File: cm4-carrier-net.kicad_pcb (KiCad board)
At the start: 4 copper layers, 91.4 x 50.4 mm, 68 parts, among them J1 USB_C_Receptacle_USB2.0, J2 Micro_SD_Card, J3 Abracon_ARJM11-502, J5 block, J6 USB_A, J8 Conn_01x15_MountingPin, Q1 DMP2066LSN, Q2 FDMT800152DC, Q3 FDMT800152DC, SW1 BOOT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

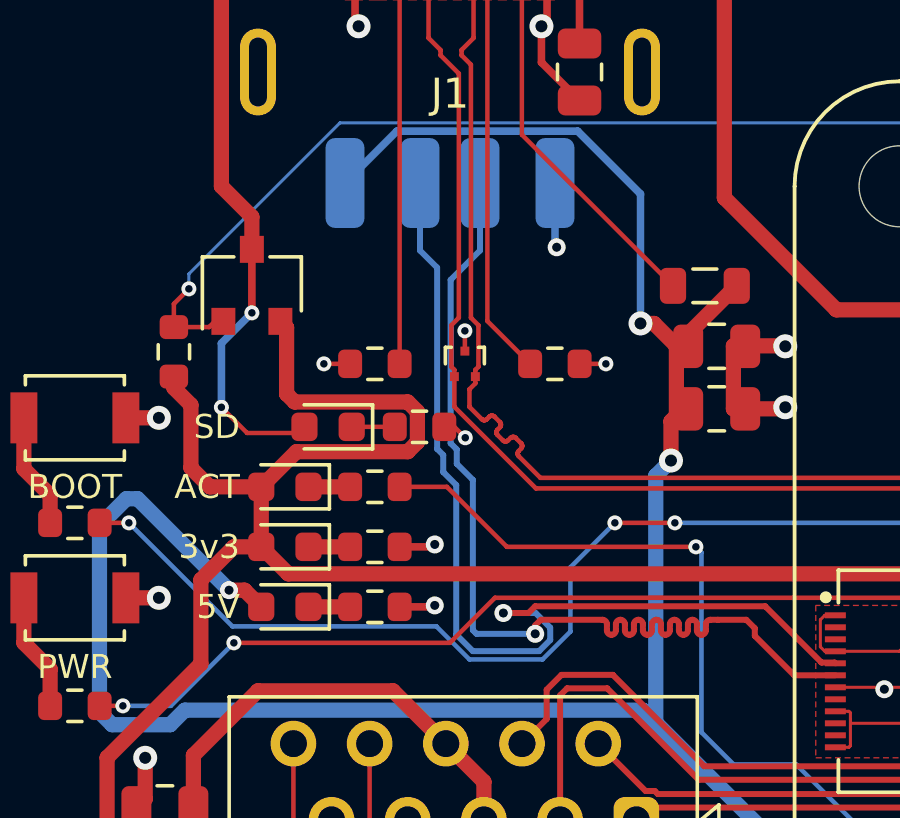
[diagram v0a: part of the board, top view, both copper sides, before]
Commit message: added tvs on the usb a
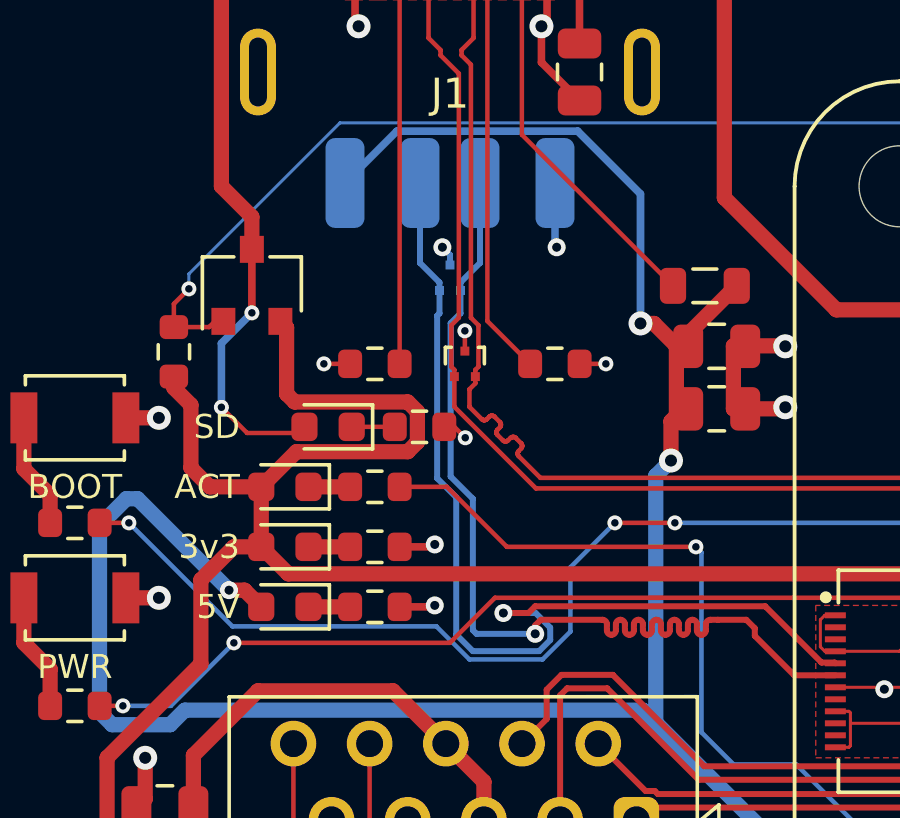
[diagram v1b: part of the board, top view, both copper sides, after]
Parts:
- added U4: TPD2EUSB30, Package_TO_SOT_SMD:Texas_DRT-3, B.Cu at (95.5, 100.3)
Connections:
- net /I2C1_SCL- renamed /I2C1_SCL0-
- net /I2C1_SDA+ renamed /I2C1_SDA0+
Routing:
- net GND: track 173.0 -> 173.7 mm, vias 55 -> 56

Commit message: added some fun thingies
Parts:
- added C12: 22u, Capacitor_SMD:C_0805_2012Metric, F.Cu at (145.8, 87.6)
- added C13: 22u, Capacitor_SMD:C_0805_2012Metric, B.Cu at (85.4, 118.4)
- added M1: Fan, Connector_PinHeader_2.54mm:PinHeader_1x02_P2.54mm_Vertical, F.Cu at (82.3, 118.4)
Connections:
- J8 pad MP: unconnected-(J8-MountPin-PadMP) -> GND
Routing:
- net +5V: track 134.1 -> 140.2 mm
- net +3.3V: track 207.3 -> 213.0 mm
- net GND: track 173.7 -> 178.3 mm, vias 56 -> 61
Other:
- board text added: "5v"
- board text added: "FAN"

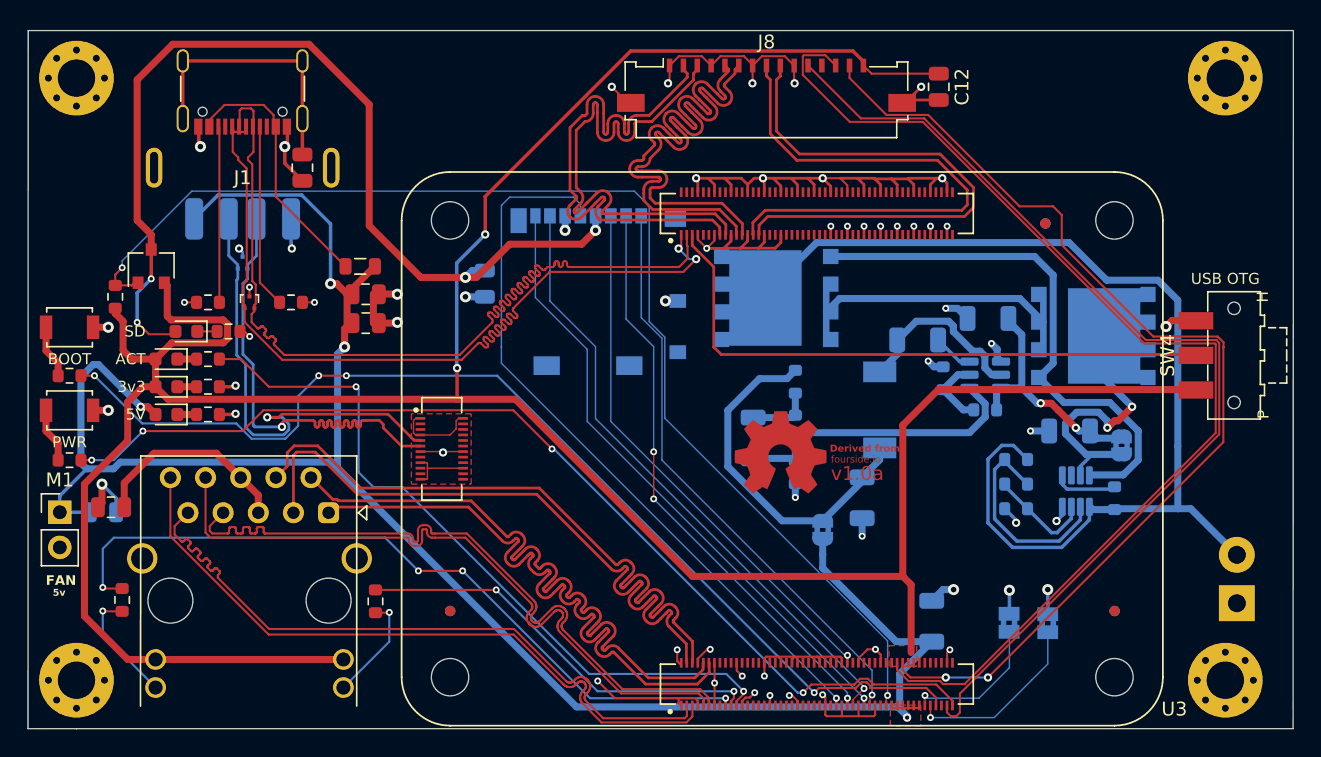
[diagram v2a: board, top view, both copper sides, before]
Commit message: redesigned pcb
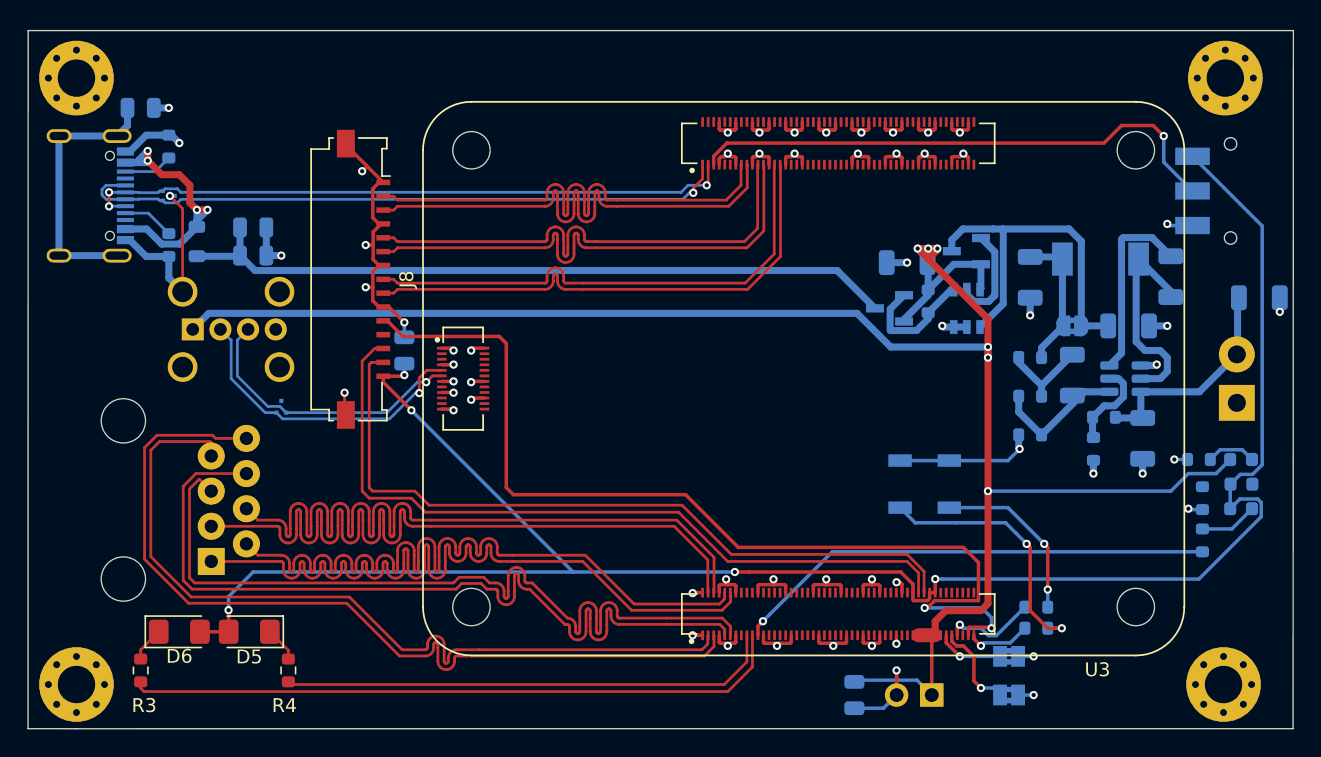
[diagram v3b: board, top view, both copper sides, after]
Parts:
- removed C3: 100n, Capacitor_SMD:C_0805_2012Metric
- removed D4: SD ON, LED_SMD:LED_0603_1608Metric
- removed FID1, FID2, FID3, FID4, FID5, FID6: Fiducial, Fiducial:Fiducial_0.75mm_Mask1.5mm
- removed J2: Micro_SD_Card, Connector_Card:microSD_HC_Molex_104031-0811
- removed JP5: SolderJumper_2_Bridged, Jumper:SolderJumper-2_P1.3mm_Bridged2Bar_RoundedPad1.0x1.5mm
- removed LOGO1: Logo_Open_Hardware_Small, Symbol:OSHW-Symbol_6.7x6mm_Copper
- removed Q1: DMP2066LSN, Package_TO_SOT_SMD:SC-59
- removed R12, R8: 220R, Resistor_SMD:R_0603_1608Metric
- removed R18: 2740kOhm, Resistor_SMD:R_0603_1608Metric
- removed R19: 215kOhm, Resistor_SMD:R_0603_1608Metric
- removed R20: 84.5kOhm, Resistor_SMD:R_0603_1608Metric
- removed U2: LTC4365TS8, Package_TO_SOT_SMD:TSOT-23-8
- added D5: LED, Diode_SMD:D_1206_3216Metric_Pad1.42x1.75mm_HandSolder, F.Cu at (96.0, 127.0)
- added D6: LED, Diode_SMD:D_1206_3216Metric_Pad1.42x1.75mm_HandSolder, F.Cu at (90.9, 127.0)
- added Q4: IRLML6401TRPBF, digikey-footprints:SOT-23-3, B.Cu at (142.2, 103.6)
- C1, C12, C2, C5, D1, D2, D3, FB1, M1, R1, R10, R11, R2, R6, R7, R9, SW1, SW2, SW4, U6: moved to B.Cu
- C4: value 22u -> 22uF; footprint Capacitor_SMD:C_0805_2012Metric -> Capacitor_SMD:C_1206_3216Metric
- J1: footprint jkiv-library:USB_C_Receptacle_GCT-USB4105 -> Connector_USB:USB_C_Receptacle_G-Switch_GT-USB-7010ASV; moved to B.Cu
- J3: value Abracon_ARJM11-502 -> 54602-908LF; footprint jkiv-library:RJ45_Abracon_ARJM11 -> digikey-footprints:Ethernet_Jack_54602-908LF; moved to B.Cu
- J6: footprint Connector_USB:USB_A_Receptacle_GCT_USB1046 -> Connector_USB:USB_A_Wuerth_614004134726_Horizontal
- Q2: value FDMT800152DC -> LTC4412ES6_TRMPBF; footprint Package_TO_SOT_SMD:PQFN_8x8 -> digikey-footprints:SOT-23-6
- Q3: value FDMT800152DC -> IRLML6401TRPBF; footprint Package_TO_SOT_SMD:PQFN_8x8 -> digikey-footprints:SOT-23-3
- R17: value 510kOhm -> 470kOhm
- moved D3 78.4 mm to (167.6, 118.1)
- moved D2 78.0 mm to (167.7, 116.3)
- moved D1 77.7 mm to (167.6, 114.6)
- moved R10 73.0 mm to (164.8, 120.4), turned to 90 degrees
- moved R7 72.3 mm to (164.8, 117.3), turned to -90 degrees
- moved R9 71.8 mm to (152.8, 125.2), turned to 180 degrees
- moved R6 71.7 mm to (164.6, 114.6), turned to 180 degrees
- moved R11 70.9 mm to (152.8, 126.7), turned to 180 degrees
- moved SW1 64.6 mm to (146.6, 116.3), turned to 90 degrees
- moved M1 64.4 mm to (145.3, 131.6), turned to 90 degrees
- moved SW2 60.2 mm to (143.0, 116.3), turned to 90 degrees
- moved C13 55.9 mm to (139.7, 131.6), turned to -90 degrees
- moved C12 43.1 mm to (107.2, 106.7), turned to 90 degrees
- moved J8 32.1 mm to (104.8, 101.5), turned to -90 degrees
- moved C4 30.5 mm to (143.5, 100.3), turned to 180 degrees
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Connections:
- C1 pad 1: +5V -> 5v_From_USB
- C10 pad 2: +5V -> 5v_From_Bot
- C2 pad 1: +5V -> 5v_From_USB
- C4 pad 1: /SD_PWR -> +5V
- FB1 pad 1: +5V -> 5v_From_USB
- J3 pad 5: Net-(C3-Pad1) -> /E0_TR2+
- J3 pad 6: Net-(C3-Pad1) -> /E0_TR2-
- J3 pad 7: /E0_TR2+ -> /E0_TR3+
- J3 pad 8: /E0_TR2- -> /E0_TR3-
- J5 pad 2: Net-(J5-Pin_2) -> +12V
- JP6 pad 1: +5V -> 5v_From_Bot
- Q2 pad 1: Net-(Q2-G) -> 5v_From_Bot
- Q2 pad 2: Net-(Q2-S) -> GND
- Q2 pad 3: Net-(J5-Pin_2) -> GND
- Q3 pad 1: Net-(Q2-G) -> Net-(Q2-GATE)
- Q3 pad 2: Net-(Q2-S) -> +5V
- Q3 pad 3: Net-(JP5-A) -> 5v_From_Bot
- R17 pad 1: Net-(J5-Pin_2) -> +5V
- R17 pad 2: Net-(U2-~{SHDN}) -> Net-(Q2-STAT)
- R3 pad 1: Net-(J3-Pad14) -> Net-(D6-K)
- R4 pad 1: Net-(J3-Pad12) -> Net-(D5-K)
- U3 pad JP2_100: unconnected-(U3B-HDMI_TXDDC_SCL_PORT-PadJP2_100) -> /HDMI_SCL
- U3 pad JP2_51: unconnected-(U3B-HDMI_CEC_PORT-PadJP2_51) -> /HDMI_CEC
- U3 pad JP2_70: unconnected-(U3B-HDMI_TX2P_PORT-PadJP2_70) -> /HDMI_D2+
- U3 pad JP2_72: unconnected-(U3B-HDMI_TX2N_PORT-PadJP2_72) -> /HDMI_D2-
- U3 pad JP2_76: unconnected-(U3B-HDMI_TX1P_PORT-PadJP2_76) -> /HDMI_D1+
- U3 pad JP2_78: unconnected-(U3B-HDMI_TX1N_PORT-PadJP2_78) -> /HDMI_D1-
- U3 pad JP2_82: unconnected-(U3B-HDMI_TX0P_PORT-PadJP2_82) -> /HDMI_D0+
- U3 pad JP2_84: unconnected-(U3B-HDMI_TX0N_PORT-PadJP2_84) -> /HDMI_D0-
- U3 pad JP2_88: unconnected-(U3B-HDMI_TXCLKP_PORT-PadJP2_88) -> /HDMI_CK+
- U3 pad JP2_90: unconnected-(U3B-HDMI_TXCLKN_PORT-PadJP2_90) -> /HDMI_CK-
- U3 pad JP2_99: unconnected-(U3B-HDMI_TXDDC_SDA_PORT-PadJP2_99) -> /HDMI_SDA
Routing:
- net /SD_PWR_ON: track 87.7 -> 0.00 mm, vias 2 -> 0
- net Net-(J5-Pin_2): track 78.6 -> 0.00 mm
- net +3.3V: track 213.0 -> 139.7 mm, vias 2 -> 5
- net /SD_PWR: track 71.9 -> 0.00 mm, vias 4 -> 0
- net /PI_nRPI_BOOT: track 77.9 -> 6.71 mm, vias 4 -> 1
- net /PI_GLOBAL_EN: track 74.5 -> 4.68 mm, vias 4 -> 1
- net /SD_CLK: track 53.4 -> 0.00 mm, vias 1 -> 0
- net 5v_From_USB: track 0.00 -> 52.6 mm
- net /SD_D1: track 45.4 -> 0.00 mm, vias 1 -> 0
- net /SD_D0: track 45.3 -> 0.00 mm, vias 1 -> 0
- net /SD_D2: track 42.5 -> 0.00 mm, vias 1 -> 0
- net /SD_D3: track 42.2 -> 0.00 mm, vias 3 -> 0
- net /SD_CMD: track 39.7 -> 0.00 mm, vias 1 -> 0
- net Net-(Q2-G): track 39.3 -> 0.00 mm
- net GND: track 178.3 -> 146.7 mm, vias 61 -> 59
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- removed copper zone on F.Cu, net +3.3V
- removed copper zone on F.Cu, net +5V
- removed copper zone on F.Cu, net GND
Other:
- board text removed: "3v3"
- board text removed: "5V"
- board text removed: "5v"
- board text removed: "ACT"
- board text removed: "BOOT"
- board text removed: "Derived from"
- board text removed: "FAN"
- board text removed: "H"
- board text removed: "P"
- board text removed: "PWR"
- board text removed: "SD"
- board text removed: "These should probably be toggles, but I don't feel like making more space for unnecessary things."
- board text removed: "USB OTG"
- board text removed: "fourside.io"
- board text removed: "v1.0a"
- board text removed: "~{BT}"
- board text removed: "~{WiFi}"
